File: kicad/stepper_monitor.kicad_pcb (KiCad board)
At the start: 2 copper layers, 44.4 x 54.5 mm, 61 parts, among them J1 Conn_01x04_Pin, J2 Conn_01x04_Pin, J3 Conn_01x02_Pin, J4 USB_C_Receptacle_USB2.0, J5 JTAG, Q1 MMDT2222A, SW1 SW_Push, U1 5V, U2 CP2102N-A01-GQFN28, U3 AMS1117-3.3, U4 CC6920BSO-5A, U5 CC6920BSO-5A, U6 ESP32-WROOM-32U-N4

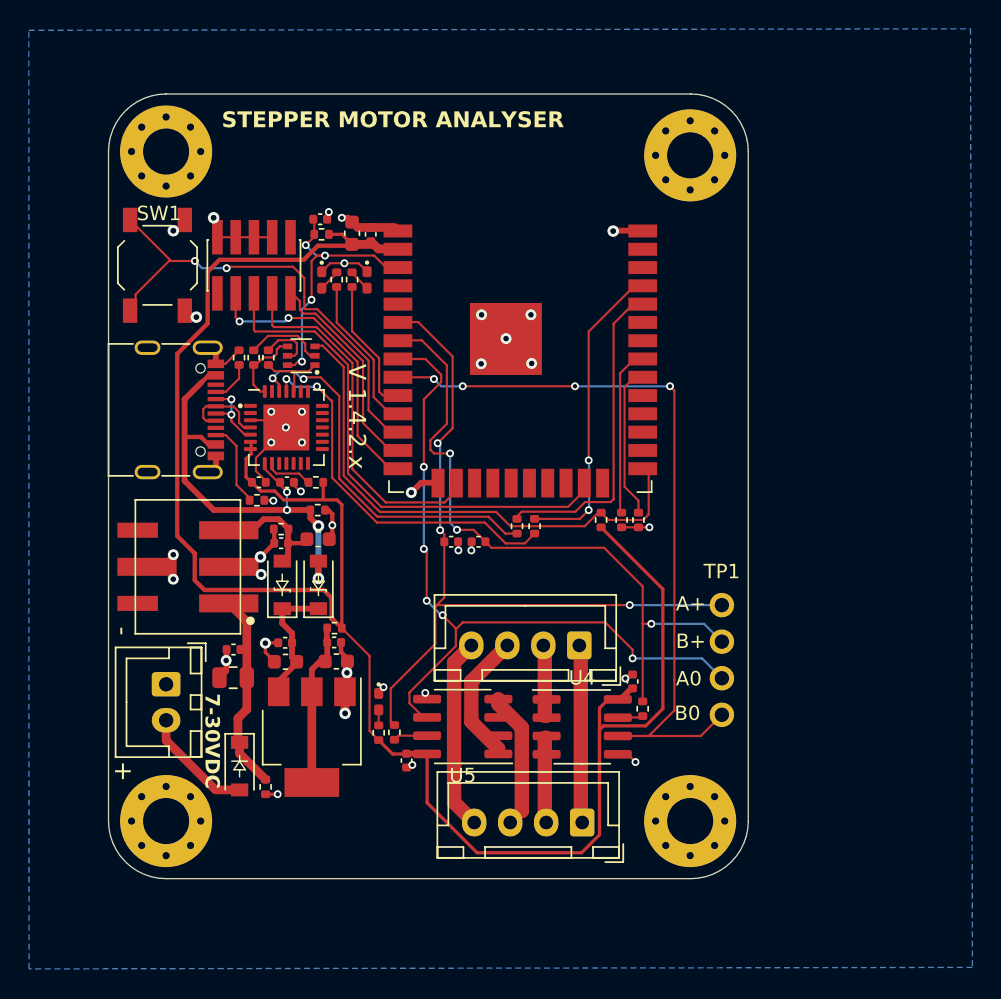
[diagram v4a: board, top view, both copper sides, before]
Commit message: Rerouted everything. Basic part LEDs. 6 pin connector. Smaller footprint. Shorter routes
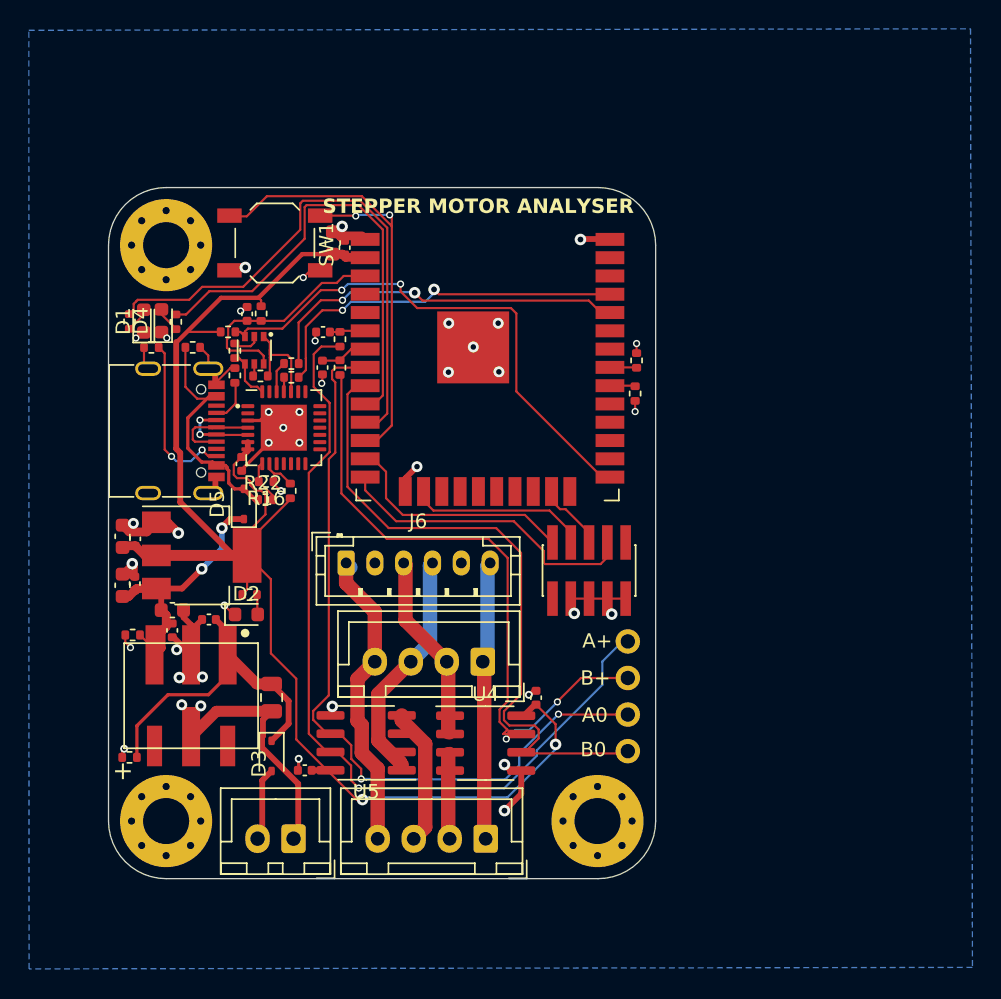
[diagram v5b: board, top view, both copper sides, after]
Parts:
- removed C4: 100n, Capacitor_SMD:C_0402_1005Metric
- removed D6: B5819W, stepper_monitor:D_SOD-123
- removed H2: MountingHole, MountingHole:MountingHole_3.2mm_M3_Pad_Via
- added J6: Conn_01x04_Pin, Connector_JST:JST_PH_B6B-PH-K_1x06_P2.00mm_Vertical, F.Cu at (16.5, -18.4)
- added R22: 5K1, Resistor_SMD:R_0402_1005Metric, F.Cu at (10.9, -22.8)
- D1: footprint stepper_monitor:LED_0402_1005Metric_Pad0.77x0.64mm_HandSolder -> LED_SMD:LED_0603_1608Metric
- D2: value GREEN -> Yellow; footprint stepper_monitor:LED_0402_1005Metric_Pad0.77x0.64mm_HandSolder -> LED_SMD:LED_0603_1608Metric
- D3: value SM4007PL -> 1N5819WS; footprint stepper_monitor:D2_SOD-123 -> Diode_SMD:D_SOD-323
- D4: value RED -> BLUE; footprint stepper_monitor:LED_0402_1005Metric_Pad0.77x0.64mm_HandSolder -> LED_SMD:LED_0603_1608Metric
- D5: value B5819W -> 1N5819WS; footprint stepper_monitor:D_SOD-123 -> Diode_SMD:D_SOD-323
- R16: value 0R -> 10K
- moved R19 31.7 mm to (16.1, -32.0)
- moved J5 31.5 mm to (33.4, -17.9), turned to 0 degrees
- moved D4 30.5 mm to (3.67, -35.2), turned to 90 degrees
- moved R13 29.0 mm to (8.30, -34.5), turned to 180 degrees
- moved R20 27.6 mm to (16.1, -34.0)
- moved D2 24.7 mm to (9.57, -14.8), turned to 0 degrees
- moved R14 19.8 mm to (12.7, -31.3), turned to 180 degrees
- moved R15 19.3 mm to (12.7, -32.3), turned to 180 degrees
- moved C10 17.2 mm to (0.97, -20.3), turned to -90 degrees
- moved C19 17.1 mm to (14.9, -34.5), turned to 180 degrees
- moved C16 16.2 mm to (14.9, -32.0), turned to -90 degrees
- moved C11 15.6 mm to (1.85, -20.1), turned to -90 degrees
- moved U3 14.8 mm to (6.47, -18.9), turned to 180 degrees
- moved R1 14.7 mm to (1.46, -35.2), turned to 90 degrees
- moved R9 14.2 mm to (5.85, -33.4)
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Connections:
- net Net-(D3-K) renamed +12V
- C10 pad 2: Net-(U3-VO) -> +3V3
- C11 pad 2: Net-(U3-VO) -> +3V3
- C3 pad 2: Net-(D6-A) -> +5V
- C5 pad 2: Net-(D6-A) -> +5V
- C6 pad 2: Net-(D5-K) -> +5V
- C8 pad 2: Net-(D5-K) -> +5V
- D5 pad 1: Net-(D5-K) -> +5V
- H1 pad 1: (no net) -> GNDD
- H3 pad 1: (no net) -> GNDD
- H4 pad 1: (no net) -> GNDD
- R16 pad 1: +3V3 -> GNDD
- R16 pad 2: Net-(U3-VO) -> Net-(U2-VBUS)
- R19 pad 2: Net-(U4-VIOUT) -> CHB_RAW
- R2 pad 1: Net-(D2-A) -> Net-(D4-A)
- R20 pad 2: Net-(U5-VIOUT) -> CHA_RAW
- R6 pad 1: Net-(D4-A) -> Net-(D2-A)
- R8 pad 2: Net-(D6-A) -> +5V
- TP1 pad 1: CHA -> CHA_RAW
- TP1 pad 2: CHB -> CHB_RAW
- U1 pad 3: Net-(D6-A) -> +5V
- U2 pad 8: VBUS -> Net-(U2-VBUS)
- U3 pad 2: Net-(U3-VO) -> +3V3
- U3 pad 3: Net-(D5-K) -> +5V
- U4 pad 7: Net-(U4-VIOUT) -> CHB_RAW
- U5 pad 7: Net-(U5-VIOUT) -> CHA_RAW
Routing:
- net CHA_RAW: track 0.00 -> 59.2 mm, vias 0 -> 1
- net CHA: track 52.6 -> 2.48 mm, vias 3 -> 0
- net CHB_RAW: track 0.00 -> 47.1 mm, vias 0 -> 2
- net CHB: track 46.0 -> 3.30 mm, vias 3 -> 0
- net ESP_TDO: track 36.0 -> 4.84 mm
- net +3V3: track 136.2 -> 106.4 mm, vias 0 -> 2
- net LED1: track 10.9 -> 37.9 mm
- net Net-(U2-RXD): track 26.3 -> 1.01 mm, vias 2 -> 0
- net Net-(U2-TXD): track 26.4 -> 2.17 mm, vias 2 -> 0
- net GNDD: track 58.9 -> 82.8 mm, vias 38 -> 41
- net LED2: track 9.46 -> 32.5 mm
- net +5V: track 0.00 -> 20.7 mm, vias 0 -> 2
- net VBUS: track 30.5 -> 16.8 mm, vias 4 -> 0
- net ESP_TCK: track 25.3 -> 12.5 mm
- net Net-(U3-VO): track 11.5 -> 0.00 mm
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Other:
- board size 44.4 x 54.5 mm -> 38 x 48 mm
- board text added: "5-30VDC"
- board text removed: "7-30VDC"
- board text removed: "V 1.4.2.x"

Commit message: Added 5V dupoint pins
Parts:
- added TP2: 5V_pins, Connector_PinHeader_2.54mm:PinHeader_1x02_P2.54mm_Vertical, F.Cu at (12.7, -19.3)
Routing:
- net +5V: track 20.7 -> 26.2 mm
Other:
- board text added: "Scope"
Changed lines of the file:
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@@
+    )
+  )
+  (footprint "Connector_PinHeader_2.54mm:PinHeader_1x02_P2.54mm_Vertical" (layer "F.Cu")
+    (at 12.65 -19.325)
+    (descr "Through hole straight pin header, 1x02, 2.54mm pitch, single row")
+    (tags "Through hole pin header THT 1x02 2.54mm single row")
+    (property "LCSC" "")
+    (property "Sheetfile" "stepper_monitor.kicad_sch")
+    (property "Sheetname" "")
+    (property "ki_description" "Generic connector, single row, 01x02, script generated")
+    (property "ki_keywords" "connector")
+    (attr through_hole)
+    (fp_text reference "TP2" (at 0 -2.33) (layer "F.SilkS")
+        (effects (font (size 1 1) (thickness 0.15)))
+    )
+    (fp_text value "5V_pins" (at 0 4.87) (layer "F.Fab")
+        (effects (font (size 1 1) (thickness 0.15)))
+    )
+    (fp_text user "${REFERENCE}" (at 0 1.27 90) (layer "F.Fab")
+        (effects (font (size 1 1) (thickness 0.15)))
+    )
+    (fp_line (start -1.33 -1.33) (end 0 -1.33)
+      (stroke (width 0.12) (type solid)) (layer "F.SilkS"))
+    (fp_line (start -1.33 0) (end -1.33 -1.33)
+      (stroke (width 0.12) (type solid)) (layer "F.SilkS"))
+    (fp_line (start -1.33 1.27) (end -1.33 3.87)
+      (stroke (width 0.12) (type solid)) (layer "F.SilkS"))
+    (fp_line (start -1.33 1.27) (end 1.33 1.27)
+      (stroke (width 0.12) (type solid)) (layer "F.SilkS"))
+    (fp_line (start -1.33 3.87) (end 1.33 3.87)
+      (stroke (width 0.12) (type solid)) (layer "F.SilkS"))
+    (fp_line (start 1.33 1.27) (end 1.33 3.87)
+      (stroke (width 0.12) (type solid)) (layer "F.SilkS"))
+    (fp_line (start -1.8 -1.8) (end -1.8 4.35)
+      (stroke (width 0.05) (type solid)) (layer "F.CrtYd"))
+    (fp_line (start -1.8 4.35) (end 1.8 4.35)
+      (stroke (width 0.05) (type solid)) (layer "F.CrtYd"))
+    (fp_line (start 1.8 -1.8) (end -1.8 -1.8)
+      (stroke (width 0.05) (type solid)) (layer "F.CrtYd"))
+    (fp_line (start 1.8 4.35) (end 1.8 -1.8)
+      (stroke (width 0.05) (type solid)) (layer "F.CrtYd"))
+    (fp_line (start -1.27 -0.635) (end -0.635 -1.27)
+      (stroke (width 0.1) (type solid)) (layer "F.Fab"))
+    (fp_line (start -1.27 3.81) (end -1.27 -0.635)
+      (stroke (width 0.1) (type solid)) (layer "F.Fab"))
+    (fp_line (start -0.635 -1.27) (end 1.27 -1.27)
+      (stroke (width 0.1) (type solid)) (layer "F.Fab"))
+    (fp_line (start 1.27 -1.27) (end 1.27 3.81)
+      (stroke (width 0.1) (type solid)) (layer "F.Fab"))
+    (fp_line (start 1.27 3.81) (end -1.27 3.81)
+      (stroke (width 0.1) (type solid)) (layer "F.Fab"))
+    (pad "1" thru_hole rect (at 0 0) (size 1.7 1.7) (drill 1) (layers "*.Cu" "*.Mask")
+      (net 83 "+5V") (pinfunction "Pin_1") (pintype "passive"))
+    (pad "2" thru_hole oval (at 0 2.54) (size 1.7 1.7) (drill 1) (layers "*.Cu" "*.Mask")
+      (net 5 "GNDD") (pinfunction "Pin_2") (pintype "passive"))
+    (model "${KICAD6_3DMODEL_DIR}/Connector_PinHeader_2.54mm.3dshapes/PinHeader_1x02_P2.54mm_Vertical.wrl"
+      (offset (xyz 0 0 0))
+      (scale (xyz 1 1 1))
+      (rotate (xyz 0 0 0))
     )
   )
@@
     )
   )
+  (gr_line (start 22.425 -14.075) (end 22.425 -17.175)
+    (stroke (width 0.12) (type default)) (layer "B.SilkS"))
+  (gr_line (start 21.025 -12.65) (end 22.425 -14.075)
+    (stroke (width 0.12) (type default)) (layer "B.SilkS"))
+  (gr_line (start 20.6 -14.7) (end 20.6 -17.125)
+    (stroke (width 0.12) (type default)) (layer "B.SilkS"))
+  (gr_line (start 23.025 -12.475) (end 20.6 -14.7)
+    (stroke (width 0.12) (type default)) (layer "B.SilkS"))
   (gr_line (start 0 -40.5) (end 0 -0.5)
     (stroke (width 0.05) (type default)) (layer "Edge.Cuts"))
@@
   (gr_text "5-30VDC" (at 11.725 -1.9) (layer "B.SilkS")
     (effects (font (size 1 1) (thickness 0.155) bold) (justify mirror))
+  )
+  (gr_text "Scope" (at 32.8 -5.5 270) (layer "B.SilkS")
+    (effects (font (size 1.5 1.5) (thickness 0.15)) (justify left bottom mirror))
   )
   (gr_text "JLCJLCJLCJLC" (at 11.5747 -5) (layer "B.SilkS")
@@
   (segment (start 22.325 -18.25) (end 22.5 -18.425) (width 1) (layer "B.Cu") (net 12))
   (segment (start 20.993076 -11.568776) (end 22.325 -12.9007) (width 1) (layer "B.Cu") (net 12))
-  (segment (start 16.5 -17.025) (end 16.5 -18.425) (width 1) (layer "F.Cu") (net 13))
-  (segment (start 18.493076 -11.568776) (end 18.493076 -15.031924) (width 1) (layer "F.Cu") (net 13))
   (segment (start 18.693076 -4.130735) (end 18.693076 0.731224) (width 1) (layer "F.Cu") (net 13))
   (segment (start 17.588276 -7.161724) (end 17.588276 -5.235535) (width 1) (layer "F.Cu") (net 13))
@@
   (segment (start 18.493076 -11.568776) (end 17.293076 -10.368776) (width 1) (layer "F.Cu") (net 13))
   (segment (start 17.293076 -7.456924) (end 17.588276 -7.161724) (width 1) (layer "F.Cu") (net 13))
-  (segment (start 18.493076 -15.031924) (end 16.5 -17.025) (width 1) (layer "F.Cu") (net 13))
   (segment (start 17.293076 -10.368776) (end 17.293076 -7.456924) (width 1) (layer "F.Cu") (net 13))
+  (segment (start 16.5 -16.625) (end 16.5 -18.425) (width 1) (layer "B.Cu") (net 13))
+  (segment (start 18.493076 -11.568776) (end 18.493076 -14.631924) (width 1) (layer "B.Cu") (net 13))
   (segment (start 16.8 -18.125) (end 16.5 -18.425) (width 1) (layer "B.Cu") (net 13))
+  (segment (start 18.493076 -14.631924) (end 16.5 -16.625) (width 1) (layer "B.Cu") (net 13))
   (segment (start 23.593076 -5.152776) (end 23.593076 0.631224) (width 1) (layer "F.Cu") (net 14))
   (segment (start 23.718076 -5.277776) (end 23.593076 -5.152776) (width 0.762) (layer "F.Cu") (net 14))
@@
   (segment (start 6.475 -18.0171) (end 7.875 -19.4171) (width 0.4064) (layer "B.Cu") (net 83))
   (segment (start 7.875 -19.4171) (end 7.875 -20.85) (width 0.4064) (layer "B.Cu") (net 83))
+  (segment (start 12.65 -19.325) (end 12.625 -19.3) (width 0.4064) (layer "B.Cu") (net 83))
+  (segment (start 9.425 -19.3) (end 7.875 -20.85) (width 0.4064) (layer "B.Cu") (net 83))
+  (segment (start 12.625 -19.3) (end 9.425 -19.3) (width 0.4064) (layer "B.Cu") (net 83))
   (segment (start 12.5072 -7.2572) (end 12.5072 -8.8428) (width 0.4064) (layer "F.Cu") (net 84))
   (segment (start 4.125 -9.275) (end 6.9403 -9.275) (width 0.2286) (layer "F.Cu") (net 84))

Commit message: Using "official" espressif footprints
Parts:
- U6: footprint stepper_monitor:ESP32-WROOM-32U -> stepper_monitor:ESP32-WROOM-32UE
- moved U6 12.7 mm to (17.3, -22.9), turned to 0 degrees
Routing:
- net GNDD: vias 41 -> 40

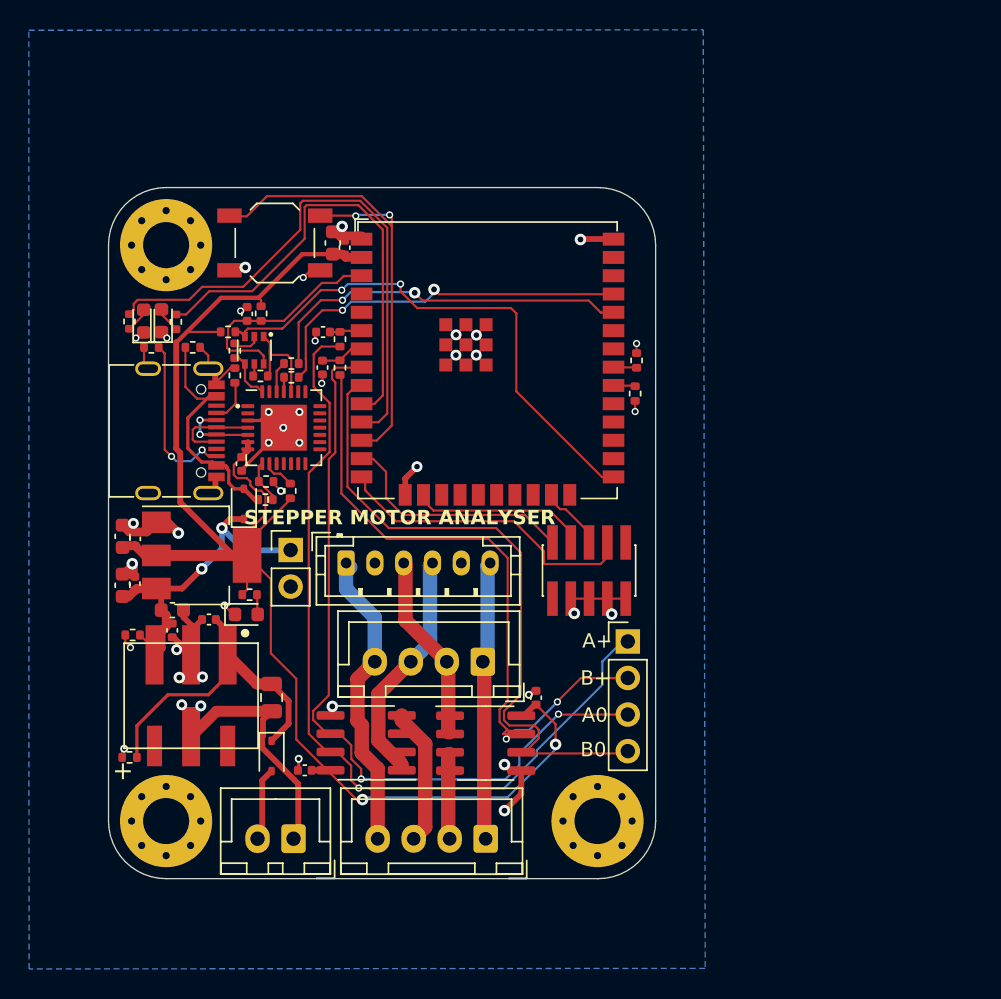
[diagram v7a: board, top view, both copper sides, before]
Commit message: Routed opamp for voltage measurement. Added 4th mount hole
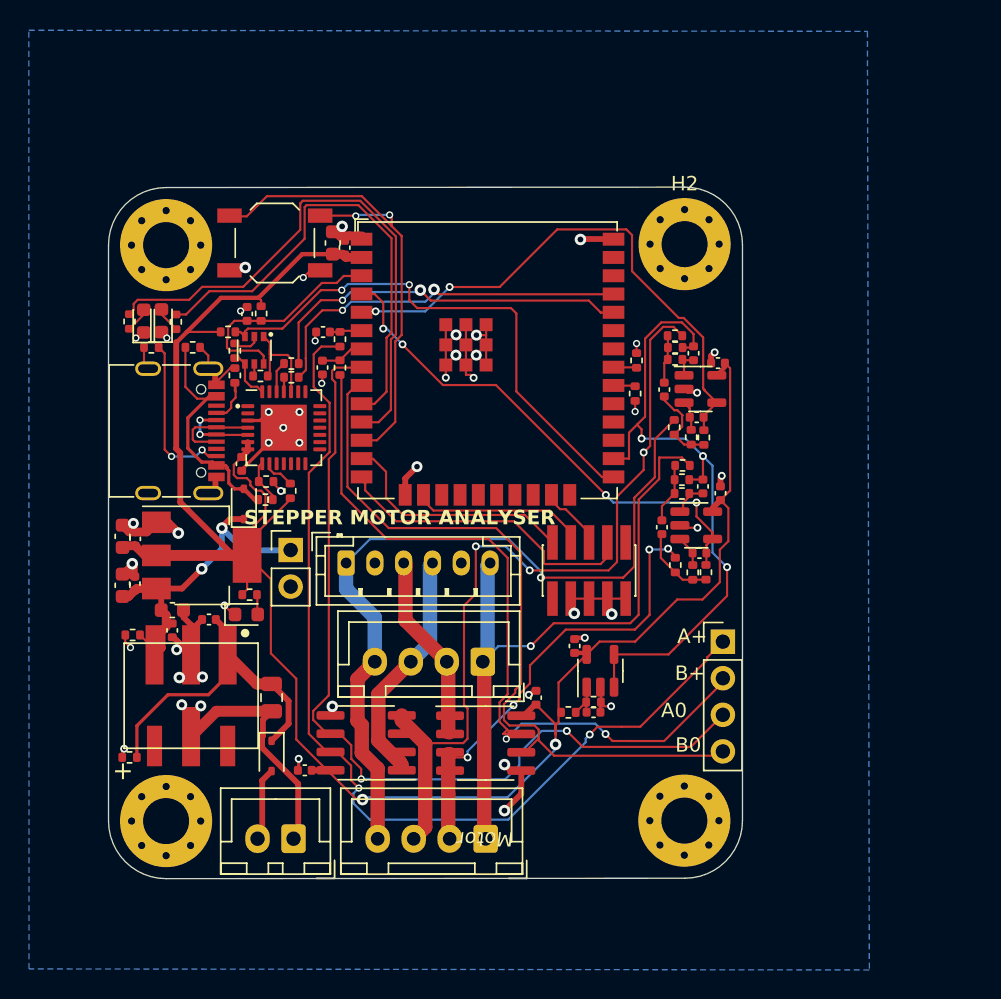
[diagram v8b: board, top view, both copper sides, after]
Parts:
- added C12: 100n, Capacitor_SMD:C_0402_1005Metric, F.Cu at (32.4, -12.7)
- added C13: 100n, Capacitor_SMD:C_0402_1005Metric, F.Cu at (33.7, -8.06)
- added C15: 100n, Capacitor_SMD:C_0402_1005Metric, F.Cu at (42.5, -23.3)
- added C16: 10n, Capacitor_SMD:C_0402_1005Metric, F.Cu at (41.3, -23.7)
- added C17: 10n, Capacitor_SMD:C_0402_1005Metric, F.Cu at (38.4, -20.9)
- added C18: 10n, Capacitor_SMD:C_0402_1005Metric, F.Cu at (41.0, -19.1)
- added C21: 100n, Capacitor_SMD:C_0402_1005Metric, F.Cu at (42.3, -32.3)
- added C22: 10n, Capacitor_SMD:C_0402_1005Metric, F.Cu at (40.6, -33.0)
- added C23: 10n, Capacitor_SMD:C_0402_1005Metric, F.Cu at (38.6, -30.5)
- added C25: 10n, Capacitor_SMD:C_0402_1005Metric, F.Cu at (40.9, -28.6)
- added H2: MountingHole, MountingHole:MountingHole_3.2mm_M3_Pad_Via, F.Cu at (40.0, -40.6)
- added R14: 1K, Resistor_SMD:R_0402_1005Metric, F.Cu at (39.8, -24.2)
- added R16: 20K, Resistor_SMD:R_0402_1005Metric, F.Cu at (39.9, -25.2)
- added R17: 10K, Resistor_SMD:R_0402_1005Metric, F.Cu at (39.8, -23.2)
- added R19: 20K, Resistor_SMD:R_0402_1005Metric, F.Cu at (39.4, -18.3)
- added R20: 10K, Resistor_SMD:R_0402_1005Metric, F.Cu at (40.6, -17.8)
- added R21: 1K, Resistor_SMD:R_0402_1005Metric, F.Cu at (41.5, -17.8)
- added R22: 1K, Resistor_SMD:R_0402_1005Metric, F.Cu at (39.4, -33.4)
- added R24: 20K, Resistor_SMD:R_0402_1005Metric, F.Cu at (39.3, -34.2)
- added R25: 10K, Resistor_SMD:R_0402_1005Metric, F.Cu at (39.4, -32.6)
- added R26: 20K, Resistor_SMD:R_0402_1005Metric, F.Cu at (39.3, -27.9)
- added R27: 10K, Resistor_SMD:R_0402_1005Metric, F.Cu at (40.5, -27.2)
- added R28: 1K, Resistor_SMD:R_0402_1005Metric, F.Cu at (41.4, -27.1)
- added R6: 1K, Resistor_SMD:R_0402_1005Metric, F.Cu at (31.9, -8.05)
- added R7: 1K, Resistor_SMD:R_0402_1005Metric, F.Cu at (33.7, -8.76)
- added U4: LMV321, Package_TO_SOT_SMD:SOT-23-5, F.Cu at (34.2, -10.9)
- added U6: LMV321, Package_TO_SOT_SMD:SOT-23-5, F.Cu at (40.8, -21.0)
- added U9: LMV321, Package_TO_SOT_SMD:SOT-23-5, F.Cu at (41.1, -30.5)
- moved TP2 6.60 mm to (42.7, -13.0)
- moved H4 6.03 mm to (40.0, -0.53)
- renumbered C12 to C1, C11 to C10, C7 to C11, C17 to C14, C13 to C2, C14 to C20, C16 to C24, C9 to C26, C1 to C3, C2 to C4, C3 to C5, C5 to C6, C6 to C7, C10 to C9, D5 to D1, D3 to D2, D1 to D3, D2 to D5, J3 to J1, J4 to J3, J6 to J4, J1 to J5, J5 to J6, R17 to R1, R15 to R10, R22 to R11, R16 to R12, R4 to R13, R5 to R15, R20 to R18, R9 to R2, R19 to R23, R12 to R29, R18 to R3, R10 to R30, R1 to R31, R2 to R32, R6 to R33, R11 to R34, R13 to R35, R3 to R4, R8 to R5, R7 to R8, R14 to R9, TP2 to TP1, TP1 to TP2, U3 to U2, U6 to U3, U2 to U5, U5 to U7, U4 to U8
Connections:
- net Net-(J1-Pin_1) renamed A1
- net Net-(J1-Pin_2) renamed A2*
- net Net-(J1-Pin_3) renamed B1*
- net Net-(J1-Pin_4) renamed B2
- net Net-(J2-Pin_2) renamed A2
- net Net-(J2-Pin_3) renamed B1
- U3 pad 26: unconnected-(U6-IO4-Pad26) -> 1.65V_ref
- U3 pad 4: unconnected-(U6-SENSOR_VP-Pad4) -> CHA_VOLT
- U3 pad 5: unconnected-(U6-SENSOR_VN-Pad5) -> CHB_VOLT
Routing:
- net B1: track 9.58 -> 57.4 mm, vias 0 -> 3
- net 1.65V_ref: track 0.00 -> 46.3 mm, vias 0 -> 3
- net CHB_VOLT: track 0.00 -> 38.0 mm, vias 0 -> 2
- net +3V3: track 106.4 -> 143.9 mm
- net CHA_VOLT: track 0.00 -> 35.3 mm, vias 0 -> 4
- net B2: track 21.5 -> 54.8 mm, vias 0 -> 1
- net A2: track 6.10 -> 33.8 mm, vias 0 -> 4
- net A1: track 19.4 -> 45.5 mm, vias 0 -> 1
- net GNDD: track 82.8 -> 106.4 mm, vias 40 -> 48
- net CHA_RAW: track 59.2 -> 67.8 mm, vias 1 -> 2
- net CHB_RAW: track 47.1 -> 54.9 mm
- net CHA_V0: track 54.8 -> 62.4 mm
- net CHB_V0: track 46.4 -> 52.4 mm
- net Net-(C23-Pad2): track 0.00 -> 5.89 mm
- net Net-(C17-Pad2): track 0.00 -> 5.45 mm
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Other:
- board size 38 x 48 mm -> 44 x 48 mm
